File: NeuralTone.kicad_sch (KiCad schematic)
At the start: 84 parts, among them J1 Power Port (5V@3A), J2 Guitar, J3 Headphone, J4 USB Port, J5 Line Out, J6 TF-01A, SW1 SW_Push, U1 MCP6022, U2 LDLN025M33R, U3 LDLN025M33R, U4 AP2151, U5 NAU8814YG, Y1 DSB211SDN 26MHz

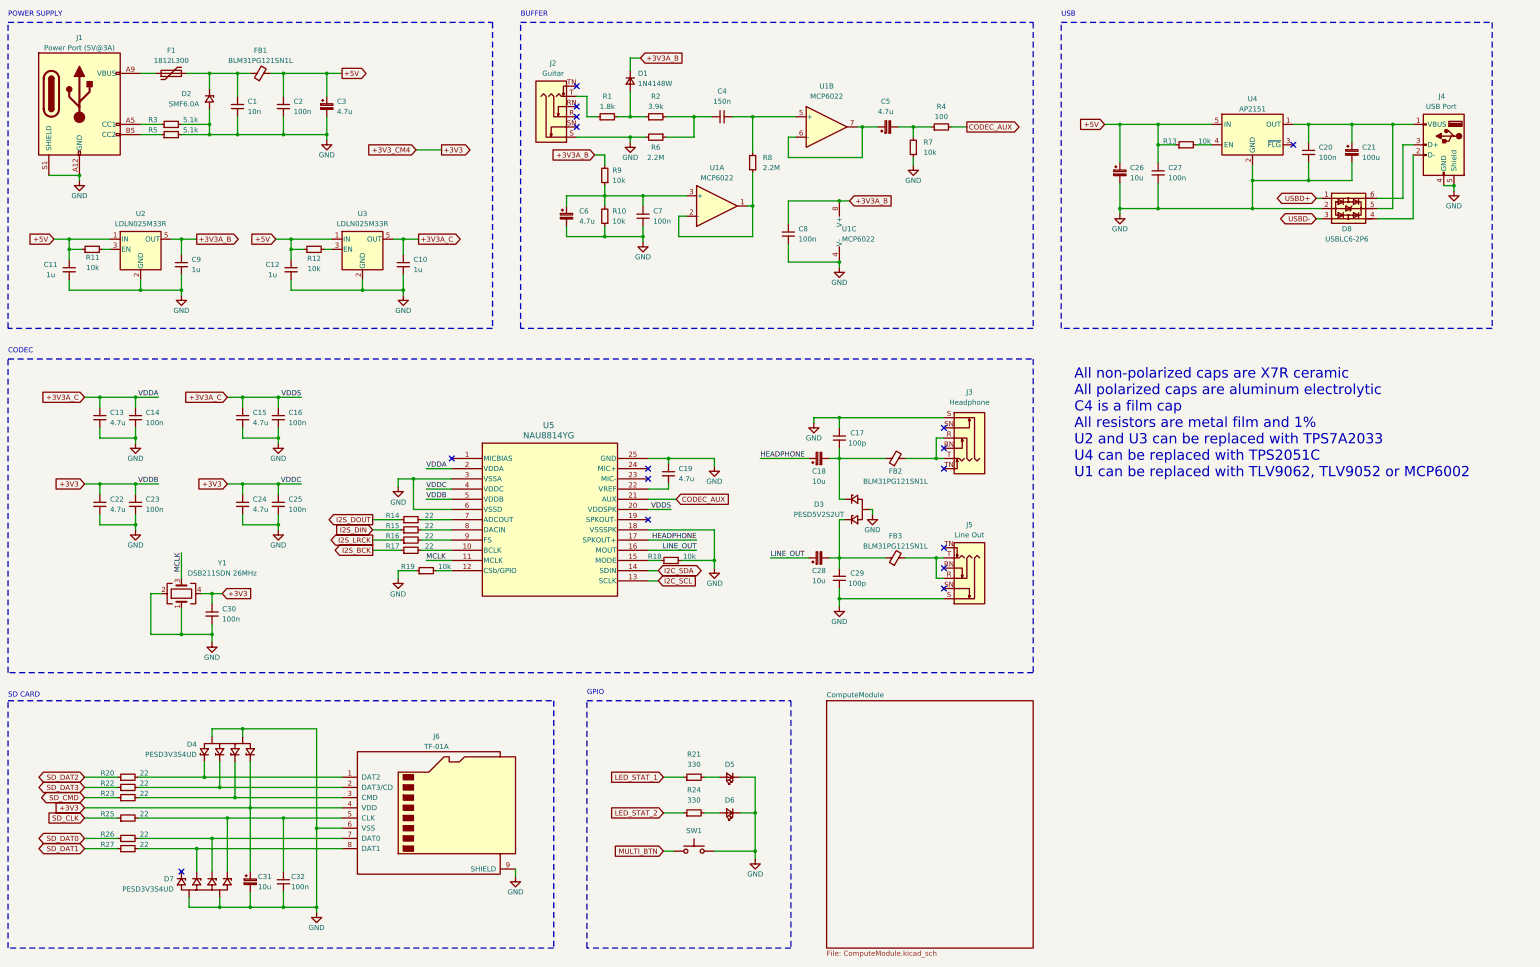
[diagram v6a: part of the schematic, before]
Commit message: better decoupling strategy
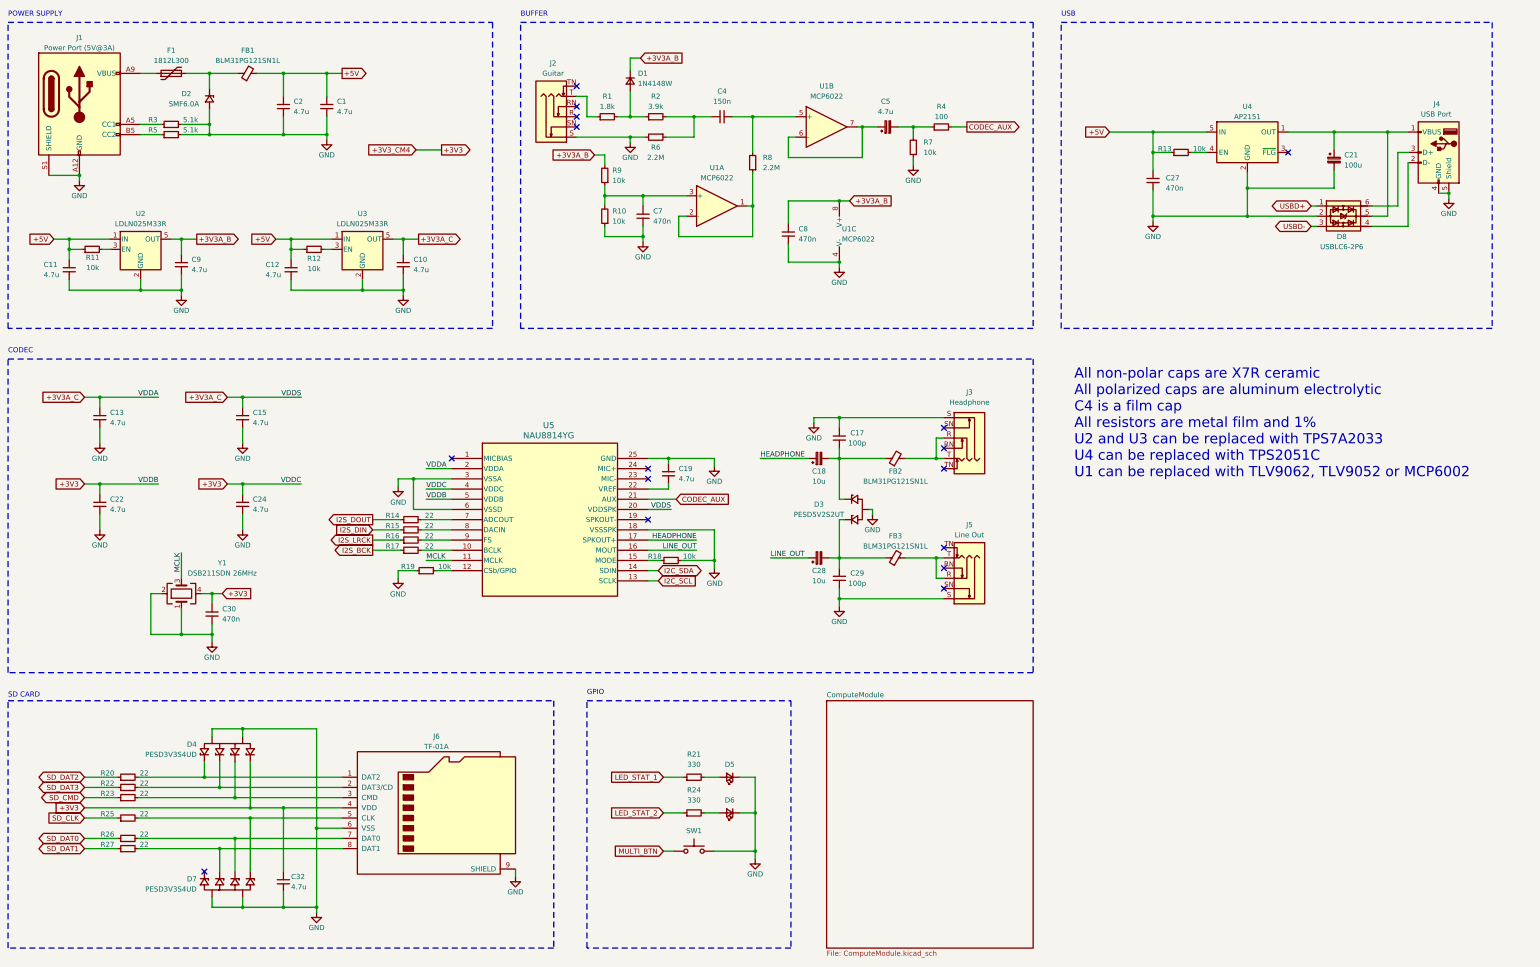
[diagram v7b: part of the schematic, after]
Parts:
- removed C14, C16, C20, C23, C25: 100n, Capacitor_SMD:C_0805_2012Metric_Pad1.18x1.45mm_HandSolder, symbol Device:C_Small
- removed C26, C31: 10u, Capacitor_SMD:CP_Elec_4x5.4, symbol Device:C_Polarized_Small
- removed C3, C6: 4.7u, Capacitor_SMD:CP_Elec_4x5.4, symbol Device:C_Polarized_Small
- C1: value 10n -> 4.7u
- C10, C11, C12, C9: value 1u -> 4.7u
- C2, C32: value 100n -> 4.7u
- C27, C30, C7, C8: value 100n -> 470n
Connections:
- net +3V3: now also C32.1
- net +5V: now also C1.1
- net at D2.1 (K), F1.2, FB1.1: no longer C1.1
- net at D7.1 (K), J6.5 (CLK), R25.2: no longer C32.1
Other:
- moved on the sheet: C21, C27, D7, D8, FB1, J4, R13, U4

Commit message: overall value adjustments
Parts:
- added C1: 10n, Capacitor_SMD:C_0805_2012Metric_Pad1.18x1.45mm_HandSolder, symbol Device:C_Small
- C4: value 150n -> 100n
- C5: value 4.7u -> 10u
- C6: renamed from C21; value 100u -> 150u; footprint Capacitor_SMD:CP_Elec_6.3x7.7 -> Capacitor_SMD:CP_Elec_6.3x5.8
- C7: renamed from C27; value 470n -> 4.7u
- R21, R24: value 330 -> 1k
- renumbered C9 to C10, C10 to C11, C11 to C12, C12 to C13, C13 to C14, C17 to C16, C18 to C17, C19 to C18, C22 to C19, C24 to C20, C28 to C21, C29 to C22, C30 to C23, C32 to C24, C1 to C3, C7 to C8, C8 to C9, D8 to D3, D3 to D4, D4 to D5, D5 to D6, D6 to D7, D7 to D8, J4 to J3, J3 to J4, R9 to R10, R10 to R11, R11 to R12, R12 to R13, R13 to R8, R8 to R9, U4 to U2, U2 to U3, U3 to U4
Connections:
- net GND: now also C1.2
- net at D2.1 (K), F1.2, FB1.1: now also C1.1
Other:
- note added: "Place close to codec"
- note added: "Place close to connector"
- note added: "Place close to connectors"
- moved on the sheet: C2, FB1
